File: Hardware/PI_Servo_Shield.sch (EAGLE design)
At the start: 46 parts, among them J1 RASPBERRYPI-40-PIN-GPIO_PTH, U1 FT231XS, U2 PCA9306, U3 PCA9685

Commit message: Changes based on talk with Adam
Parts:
- added FD1, FD2: FIDUCIALUFIDUCIAL, SparkFun-Aesthetics:FIDUCIALUFIDUCIAL
- added LOGO1: SFE_LOGO_NAME_FLAME.1_INCH, SparkFun-Aesthetics:SFE_LOGO_NAME_FLAME.1_INCH
- added LOGO2: OSHW-LOGOM, SparkFun-Aesthetics:OSHW-LOGOM
- J1: value RASPBERRYPI-40-PIN-GPIO_PTH -> RASPBERRYPI-40-PIN-GPIO_PTH_NO_SHROUD; device SparkFun-Connectors:RASPBERRYPI-40-PIN-GPIO_PTH -> SparkFun-Connectors:RASPBERRYPI-40-PIN-GPIO_PTH_NO_SHROUD

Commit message: Changes from review feedback
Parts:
- added FD3, FD4: FIDUCIALUFIDUCIAL, SparkFun-Aesthetics:FIDUCIALUFIDUCIAL
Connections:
- new net SHIELD: J2.SHIELD
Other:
- note added: "Clear this jumper to disconnect servo power from Pi power rail"
- note added: "PWM Control"
- note added: "Raspberry Pi Header"
- note added: "Serial comms"
- note added: "Servo Connections"
- moved on the sheet: C1, C2, D1, D2, J1, J2, JP1, R1, R2, R3, R4, R5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

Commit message: Addressed errors from double check
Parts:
- D1: value Yellow -> GREEN; device SparkFun-LED:LED-YELLOW0603-SMART -> SparkFun-LED:LED-GREEN0603
- D2: value Red -> Yellow; device SparkFun-LED:LED-RED0603-SMART -> SparkFun-LED:LED-YELLOW0603-SMART
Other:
- note added: "I2C Addr 0x40"
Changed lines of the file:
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@@
 <part name="GND2" library="SparkFun-PowerSymbols" deviceset="GND" device=""/>
 <part name="GND3" library="SparkFun-PowerSymbols" deviceset="GND" device=""/>
-<part name="D1" library="SparkFun-LED" deviceset="LED-YELLOW" device="0603-SMART" value="Yellow"/>
-<part name="D2" library="SparkFun-LED" deviceset="LED-RED" device="0603-SMART" value="Red"/>
+<part name="D1" library="SparkFun-LED" deviceset="LED-GREEN" device="0603" value="GREEN"/>
+<part name="D2" library="SparkFun-LED" deviceset="LED-YELLOW" device="0603-SMART" value="Yellow"/>
 <part name="R6" library="SparkFun-Resistors" deviceset="1KOHM" device="-0603-1/10W-1%" value="1k"/>
 <part name="R7" library="SparkFun-Resistors" deviceset="1KOHM" device="-0603-1/10W-1%" value="1k"/>
@@
 <text x="200.66" y="121.92" size="1.27" layer="97">Clear this jumper to disconnect
 servo power from Pi power rail</text>
+<text x="134.62" y="170.18" size="1.778" layer="97">I2C Addr 0x40</text>
 </plain>
 <instances>

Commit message: Change version number
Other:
- note added: "10"
- note removed: "00"
- moved on the sheet: C3, C4, C5, C6, C7, C8
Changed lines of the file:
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@@
 <plain>
 <text x="167.64" y="7.62" size="3.81" layer="97">M. Hord</text>
-<text x="238.76" y="6.604" size="3.81" layer="97">00</text>
+<text x="238.76" y="6.604" size="3.81" layer="97">10</text>
 <wire x1="0" y1="88.9" x2="111.76" y2="88.9" width="0.3048" layer="97" style="longdash"/>
 <wire x1="111.76" y1="88.9" x2="147.32" y2="88.9" width="0.3048" layer="97" style="longdash"/>
@@
 <instance part="C2" gate="G$1" x="35.56" y="58.42"/>
 <instance part="J2" gate="G$1" x="15.24" y="66.04" rot="MR0"/>
-<instance part="C3" gate="G$1" x="88.9" y="12.7"/>
+<instance part="C3" gate="G$1" x="81.28" y="15.24"/>
 <instance part="GND4" gate="1" x="22.86" y="48.26"/>
 <instance part="GND5" gate="1" x="58.42" y="40.64"/>
@@
 <instance part="H3" gate="G$1" x="241.3" y="27.94"/>
 <instance part="H4" gate="G$1" x="246.38" y="27.94"/>
-<instance part="GND11" gate="1" x="88.9" y="2.54"/>
-<instance part="C4" gate="G$1" x="111.76" y="12.7"/>
-<instance part="C5" gate="G$1" x="132.08" y="15.24"/>
-<instance part="SUPPLY1" gate="G$1" x="132.08" y="22.86"/>
+<instance part="GND11" gate="1" x="81.28" y="5.08"/>
+<instance part="C4" gate="G$1" x="104.14" y="15.24"/>
+<instance part="C5" gate="G$1" x="124.46" y="17.78"/>
+<instance part="SUPPLY1" gate="G$1" x="124.46" y="25.4"/>
 <instance part="JP1" gate="G$1" x="190.5" y="121.92"/>
-<instance part="C6" gate="G$1" x="142.24" y="12.7"/>
+<instance part="C6" gate="G$1" x="134.62" y="15.24"/>
 <instance part="SUPPLY2" gate="G$1" x="182.88" y="124.46"/>
-<instance part="C7" gate="G$1" x="99.06" y="12.7"/>
-<instance part="C8" gate="G$1" x="121.92" y="12.7"/>
+<instance part="C7" gate="G$1" x="91.44" y="15.24"/>
+<instance part="C8" gate="G$1" x="114.3" y="15.24"/>
 <instance part="FD1" gate="G$1" x="238.76" y="27.94"/>
 <instance part="FD2" gate="G$1" x="238.76" y="25.4"/>
@@
 <pinref part="GND11" gate="1" pin="GND"/>
 <pinref part="C3" gate="G$1" pin="2"/>
-<wire x1="88.9" y1="5.08" x2="88.9" y2="7.62" width="0.1524" layer="91"/>
+<wire x1="81.28" y1="7.62" x2="81.28" y2="10.16" width="0.1524" layer="91"/>
 <pinref part="C4" gate="G$1" pin="2"/>
-<wire x1="88.9" y1="7.62" x2="88.9" y2="10.16" width="0.1524" layer="91"/>
-<wire x1="88.9" y1="7.62" x2="99.06" y2="7.62" width="0.1524" layer="91"/>
-<wire x1="99.06" y1="7.62" x2="111.76" y2="7.62" width="0.1524" layer="91"/>
-<wire x1="111.76" y1="7.62" x2="111.76" y2="10.16" width="0.1524" layer="91"/>
-<junction x="88.9" y="7.62"/>
+<wire x1="81.28" y1="10.16" x2="81.28" y2="12.7" width="0.1524" layer="91"/>
+<wire x1="81.28" y1="10.16" x2="91.44" y2="10.16" width="0.1524" layer="91"/>
+<wire x1="91.44" y1="10.16" x2="104.14" y2="10.16" width="0.1524" layer="91"/>
+<wire x1="104.14" y1="10.16" x2="104.14" y2="12.7" width="0.1524" layer="91"/>
+<junction x="81.28" y="10.16"/>
 <pinref part="C5" gate="G$1" pin="-"/>
-<wire x1="111.76" y1="7.62" x2="121.92" y2="7.62" width="0.1524" layer="91"/>
-<wire x1="121.92" y1="7.62" x2="132.08" y2="7.62" width="0.1524" layer="91"/>
-<wire x1="132.08" y1="7.62" x2="132.08" y2="10.16" width="0.1524" layer="91"/>
-<junction x="111.76" y="7.62"/>
+<wire x1="104.14" y1="10.16" x2="114.3" y2="10.16" width="0.1524" layer="91"/>
+<wire x1="114.3" y1="10.16" x2="124.46" y2="10.16" width="0.1524" layer="91"/>
+<wire x1="124.46" y1="10.16" x2="124.46" y2="12.7" width="0.1524" layer="91"/>
+<junction x="104.14" y="10.16"/>
 <pinref part="C6" gate="G$1" pin="2"/>
-<wire x1="132.08" y1="7.62" x2="142.24" y2="7.62" width="0.1524" layer="91"/>
-<wire x1="142.24" y1="7.62" x2="142.24" y2="10.16" width="0.1524" layer="91"/>
-<junction x="132.08" y="7.62"/>
+<wire x1="124.46" y1="10.16" x2="134.62" y2="10.16" width="0.1524" layer="91"/>
+<wire x1="134.62" y1="10.16" x2="134.62" y2="12.7" width="0.1524" layer="91"/>
+<junction x="124.46" y="10.16"/>
 <pinref part="C7" gate="G$1" pin="2"/>
-<wire x1="99.06" y1="10.16" x2="99.06" y2="7.62" width="0.1524" layer="91"/>
-<junction x="99.06" y="7.62"/>
+<wire x1="91.44" y1="12.7" x2="91.44" y2="10.16" width="0.1524" layer="91"/>
+<junction x="91.44" y="10.16"/>
 <pinref part="C8" gate="G$1" pin="2"/>
-<wire x1="121.92" y1="10.16" x2="121.92" y2="7.62" width="0.1524" layer="91"/>
-<junction x="121.92" y="7.62"/>
+<wire x1="114.3" y1="12.7" x2="114.3" y2="10.16" width="0.1524" layer="91"/>
+<junction x="114.3" y="10.16"/>
 </segment>
 </net>
@@
 <pinref part="SUPPLY1" gate="G$1" pin="VIN"/>
 <pinref part="C5" gate="G$1" pin="+"/>
-<wire x1="132.08" y1="22.86" x2="132.08" y2="20.32" width="0.1524" layer="91"/>
+<wire x1="124.46" y1="25.4" x2="124.46" y2="22.86" width="0.1524" layer="91"/>
 <pinref part="C6" gate="G$1" pin="1"/>
-<wire x1="132.08" y1="20.32" x2="132.08" y2="17.78" width="0.1524" layer="91"/>
-<wire x1="132.08" y1="20.32" x2="142.24" y2="20.32" width="0.1524" layer="91"/>
-<wire x1="142.24" y1="20.32" x2="142.24" y2="17.78" width="0.1524" layer="91"/>
-<junction x="132.08" y="20.32"/>
+<wire x1="124.46" y1="22.86" x2="124.46" y2="20.32" width="0.1524" layer="91"/>
+<wire x1="124.46" y1="22.86" x2="134.62" y2="22.86" width="0.1524" layer="91"/>
+<wire x1="134.62" y1="22.86" x2="134.62" y2="20.32" width="0.1524" layer="91"/>
+<junction x="124.46" y="22.86"/>
 </segment>
 <segment>
@@
 <segment>
 <pinref part="C3" gate="G$1" pin="1"/>
-<label x="88.9" y="20.32" size="1.27" layer="95" rot="R90" xref="yes"/>
-<wire x1="88.9" y1="17.78" x2="88.9" y2="20.32" width="0.1524" layer="91"/>
+<label x="81.28" y="22.86" size="1.27" layer="95" rot="R90" xref="yes"/>
+<wire x1="81.28" y1="20.32" x2="81.28" y2="22.86" width="0.1524" layer="91"/>
 </segment>
 </net>
@@
 <segment>
 <pinref part="C4" gate="G$1" pin="1"/>
-<wire x1="111.76" y1="17.78" x2="111.76" y2="20.32" width="0.1524" layer="91"/>
-<label x="111.76" y="22.86" size="1.27" layer="95" rot="R90" xref="yes"/>
+<wire x1="104.14" y1="20.32" x2="104.14" y2="22.86" width="0.1524" layer="91"/>
+<label x="104.14" y="25.4" size="1.27" layer="95" rot="R90" xref="yes"/>
 <pinref part="C8" gate="G$1" pin="1"/>
-<wire x1="111.76" y1="20.32" x2="111.76" y2="22.86" width="0.1524" layer="91"/>
-<wire x1="111.76" y1="20.32" x2="121.92" y2="20.32" width="0.1524" layer="91"/>
-<wire x1="121.92" y1="20.32" x2="121.92" y2="17.78" width="0.1524" layer="91"/>
-<junction x="111.76" y="20.32"/>
+<wire x1="104.14" y1="22.86" x2="104.14" y2="25.4" width="0.1524" layer="91"/>
+<wire x1="104.14" y1="22.86" x2="114.3" y2="22.86" width="0.1524" layer="91"/>
+<wire x1="114.3" y1="22.86" x2="114.3" y2="20.32" width="0.1524" layer="91"/>
+<junction x="104.14" y="22.86"/>
 </segment>
 </net>
@@
 <segment>
 <pinref part="C7" gate="G$1" pin="1"/>
-<wire x1="99.06" y1="20.32" x2="99.06" y2="17.78" width="0.1524" layer="91"/>
-<label x="99.06" y="20.32" size="1.27" layer="95" rot="R90" xref="yes"/>
-</segment>
-</net>
+<wire x1="91.44" y1="22.86" x2="91.44" y2="20.32" width="0.1524" layer="91"/>
+<label x="91.44" y="22.86" size="1.27" layer="95" rot="R90" xref="yes"/>
+</segment>
+</net>

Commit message: Change to v10
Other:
- moved on the sheet: C1, C2, D1, D2, J2, R6, R7, R8, R9, U1

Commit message: v20 hardwaer 99% done - still needs buzzard migration
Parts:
- removed C1, C2: 47pF, SparkFun-Capacitors:47PF-0603-50V-5%
- removed D1: GREEN, SparkFun-LED:LED-GREEN0603
- removed D2: Yellow, SparkFun-LED:LED-YELLOW0603-SMART
- removed J2: (no value), SparkFun-Connectors:USB_MICRO-B_FEMALE-SMT
- removed R6, R7: 1k, SparkFun-Resistors:1KOHM-0603-1/10W-1%
- removed R8, R9: 27, SparkFun-Resistors:27OHM-0603-1/10W-1%
- removed U1: FT231XS, SparkFun-IC-Comms:FT231XS
- added C10: 0.1uF, SparkFun-Capacitors:0.1UF-0603-25V-(+80/-20%)
- added C17: 10nF, SparkFun-Capacitors:10NF-0603-50V-10%
- added D3: Yellow, SparkFun-LED:LED-YELLOW_HIDDENSILK
- added D4: GREEN, SparkFun-LED:LED-GREENLILYPAD
- added F2: 6V/2A, SparkFun-Fuses:PPTC_6V2A
- added J19: (no value), SparkFun-Connectors:QWIIC_CONNECTORJS-1MM
- added J20: USB C, USB-C:USB_C16PIN
- added J21: (no value), SparkFun-Connectors:CONN_04PTH
- added JP2: JUMPER-SMT_2_NO_SILK, SparkFun-Jumpers:JUMPER-SMT_2_NO_SILK
- added JP3: I2C, SparkFun-Jumpers:JUMPER-SMT_3_2-NC_TRACE_SILK
- added R10, R11: 5.1k, SparkFun-Resistors:5.1KOHM5.1KOHM-0603-1/10W-1%
- added R12, R16: 4.7k, SparkFun-Resistors:4.7KOHM-0603-1/10W-1%
- added U$1: QWIIC_LOGO_3MM, SparkFun-Aesthetics:QWIIC_LOGO_3MM
- added U5: CH340C, SparkFun-IC-Comms:CH340C
- JP1: value JUMPER-SMT_2_NC_PASTE_NO-SILK -> VIN ISO
- LOGO2: value OSHW-LOGOM -> OSHW-LOGOS; device SparkFun-Aesthetics:OSHW-LOGOM -> SparkFun-Aesthetics:OSHW-LOGOS
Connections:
- removed net N$10: C2.1, J2.D+, R9.1
- removed net N$11: C1.1, J2.D-, R8.1
- removed net N$6: D1.C, R6.2
- removed net N$7: R7.1, U1.CBUS1
- removed net N$8: R6.1, U1.CBUS2
- removed net N$9: R9.2, U1.USBDP
- removed net RXD: J1.TXO, U1.RXD
- removed net SHIELD: J2.SHIELD
- removed net TXD: J1.RXI, U1.TXD
- new net CC1: J20.CC1, R11.2
- new net CC2: J20.CC2, R10.2
- new net D+: J20.D+, U5.UD+
- new net D-: J20.D-, U5.UD-
- new net N$12: D4.A, R16.1
- new net N$13: D3.A, R12.1
- new net N$14: C17.1, U5.V3
- new net RXI: D4.C, J1.TXO, J21.1, U5.RXI
- new net SHLD: J20.SHLD
- new net TXO: D3.C, J1.RXI, J21.2, U5.TXO
- new net VBUS: C10.1, F2.1, J20.VBUS, JP2.1
- net 3.3VA: now also R12.2, R16.2, U5.VCC; no longer D1.A, D2.A, U1.!RESET, U1.VCCIO
- net 3.3VB: now also J19.2, JP3.2; no longer R4.2, R5.2
- net 5VB: now also J21.4; no longer U1.VCC
- net GND: now also C10.2, C17.2, J19.1, J20.GND, J21.3, R10.1, R11.1, U5.GND; no longer C1.2, C2.2, J2.GND, U1.GND@16, U1.GND@6
- net LV_SCL: now also J19.4
- net LV_SDA: now also J19.3
- net N$2: now also JP3.3, R4.2; no longer R8.2, U1.USBDM
- net N$5: now also JP3.1, R5.2; no longer D2.C, R7.2
- net VIN: now also F2.2, JP2.2; no longer J2.VBUS
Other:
- note added: "Pete Lewis"
- note added: "Revised by:"
- note added: "This is the penny-in-the-fuse jumper. Close only if you know what you're doing."
- note added: "USB-to-Serial Converter"
- note added: "v20"
- note removed: "10"
- note removed: "Serial comms"
- moved on the sheet: JP1, R1, R2, R3, R4, R5, U2, U3

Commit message: Buzzard migration complete
Also nudged some stuff to avoid silk on vias and to make room for a few labels.
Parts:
- JP1: device SparkFun-Jumpers:JUMPER-SMT_2_NC_PASTE_NO-SILK -> SparkFun-Jumpers:JUMPER-SMT_2_NC_PASTE_SILK
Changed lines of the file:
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@@
 <part name="C5" library="SparkFun-Capacitors" deviceset="100UF-POLAR" device="-25V-20%(ELEC)" value="100uF"/>
 <part name="SUPPLY1" library="SparkFun-PowerSymbols" deviceset="VIN" device=""/>
-<part name="JP1" library="SparkFun-Jumpers" deviceset="JUMPER-SMT_2_NC_PASTE" device="_NO-SILK" value="VIN ISO"/>
+<part name="JP1" library="SparkFun-Jumpers" deviceset="JUMPER-SMT_2_NC_PASTE" device="_SILK" value="VIN ISO"/>
 <part name="C6" library="SparkFun-Capacitors" deviceset="0.1UF" device="-0603-25V-5%" value="0.1uF"/>
 <part name="SUPPLY2" library="SparkFun-PowerSymbols" deviceset="VIN" device=""/>

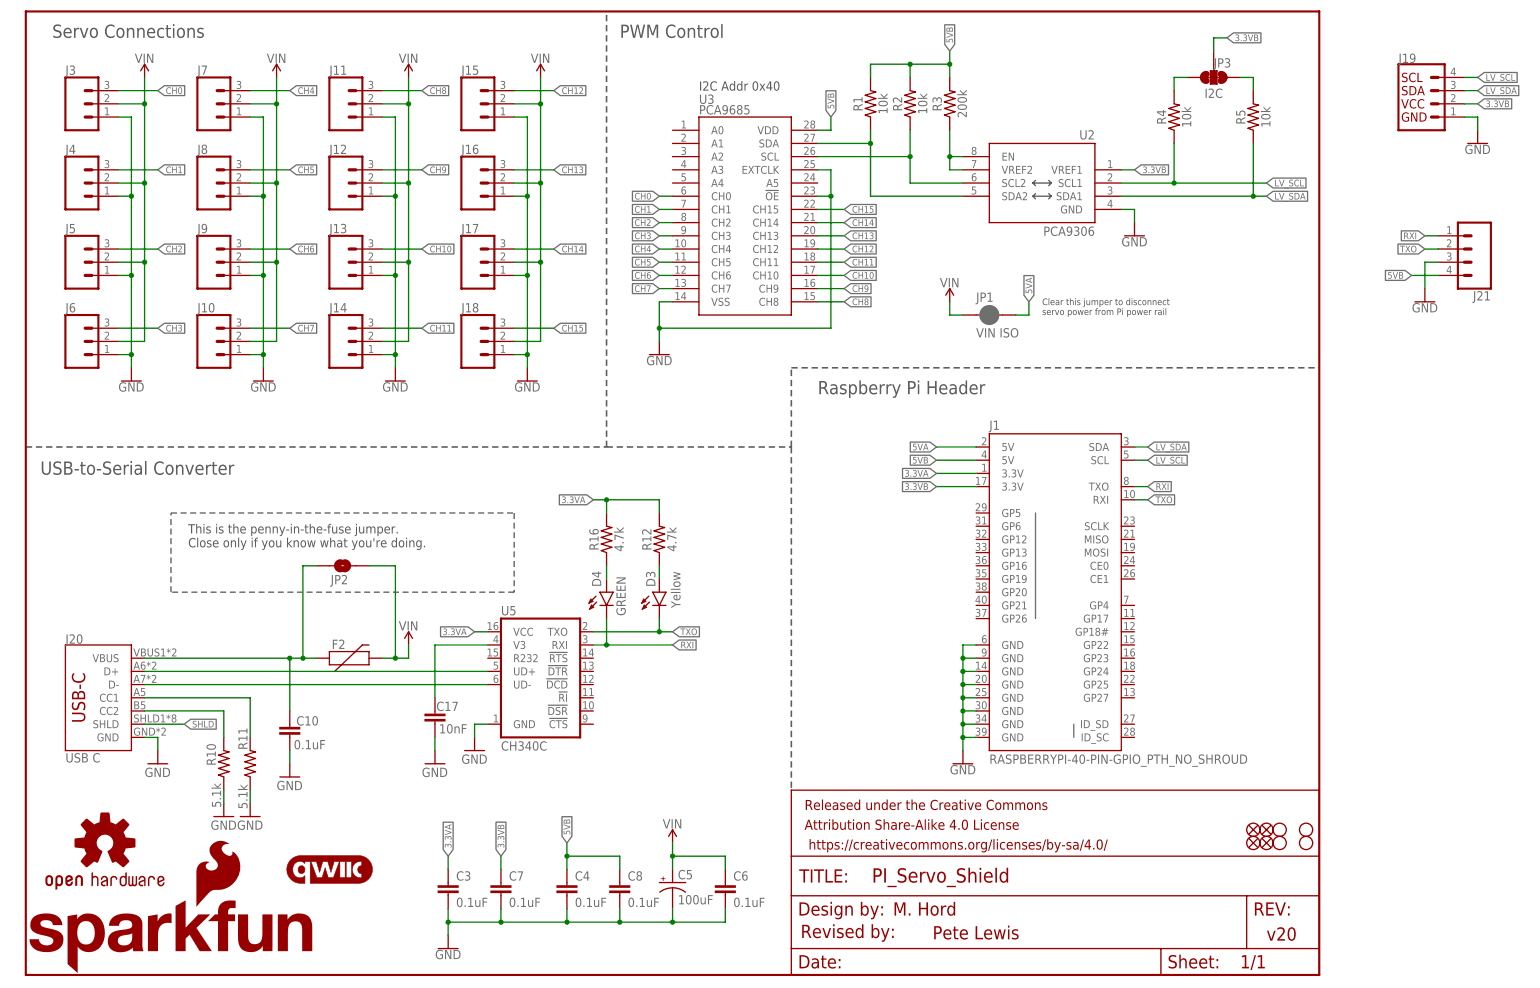
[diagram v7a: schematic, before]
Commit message: locking fp on serial header, sch cleanup
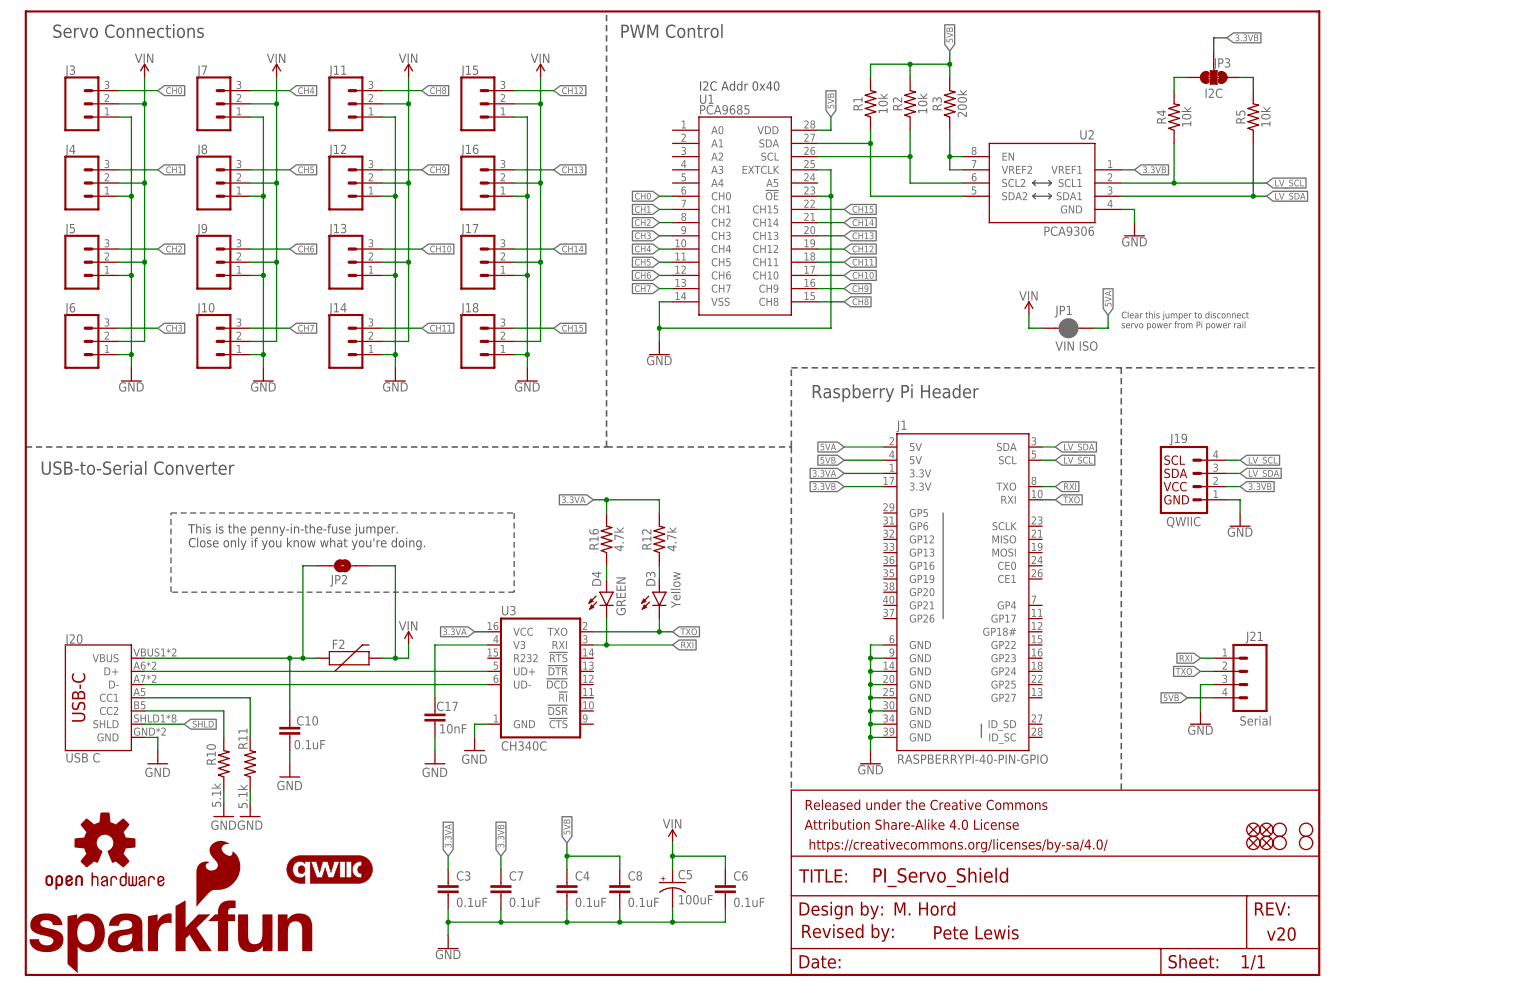
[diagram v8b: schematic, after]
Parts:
- removed U5: CH340C, SparkFun-IC-Comms:CH340C
- added U1: PCA9685, SparkFun-IC-Special-Function:PCA9685
- J1: value RASPBERRYPI-40-PIN-GPIO_PTH_NO_SHROUD -> RASPBERRYPI-40-PIN-GPIO
- J19: value (none) -> QWIIC
- J21: value (none) -> Serial; device SparkFun-Connectors:CONN_04PTH -> SparkFun-Connectors:CONN_04LOCK
- U3: value PCA9685 -> CH340C; device SparkFun-IC-Special-Function:PCA9685 -> SparkFun-IC-Comms:CH340C
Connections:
- net 3.3VA: now also U3.VCC; no longer U5.VCC
- net 5VB: now also U1.VDD; no longer U3.VDD
- net CH0: now also U1.CH0; no longer U3.CH0
- net CH1: now also U1.CH1; no longer U3.CH1
- net CH10: now also U1.CH10; no longer U3.CH10
- net CH11: now also U1.CH11; no longer U3.CH11
- net CH12: now also U1.CH12; no longer U3.CH12
- net CH13: now also U1.CH13; no longer U3.CH13
- net CH14: now also U1.CH14; no longer U3.CH14
- net CH15: now also U1.CH15; no longer U3.CH15
- net CH2: now also U1.CH2; no longer U3.CH2
- net CH3: now also U1.CH3; no longer U3.CH3
- net CH4: now also U1.CH4; no longer U3.CH4
- net CH5: now also U1.CH5; no longer U3.CH5
- net CH6: now also U1.CH6; no longer U3.CH6
- net CH7: now also U1.CH7; no longer U3.CH7
- net CH8: now also U1.CH8; no longer U3.CH8
- net CH9: now also U1.CH9; no longer U3.CH9
- net D+: now also U3.UD+; no longer U5.UD+
- net D-: now also U3.UD-; no longer U5.UD-
- net GND: now also U1.!OE, U1.EXTCLK, U1.VSS, U3.GND; no longer U3.!OE, U3.EXTCLK, U3.VSS, U5.GND
- net N$14: now also U3.V3; no longer U5.V3
- net N$3: now also U1.SCL; no longer U3.SCL
- net N$4: now also U1.SDA; no longer U3.SDA
- net RXI: now also U3.RXI; no longer U5.RXI
- net TXO: now also U3.TXO; no longer U5.TXO
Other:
- moved on the sheet: J1, J19, J21, JP1
